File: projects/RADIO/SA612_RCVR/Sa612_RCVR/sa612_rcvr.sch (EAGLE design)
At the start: 33 parts, among them IC1 SA612AN, Q1 BC238

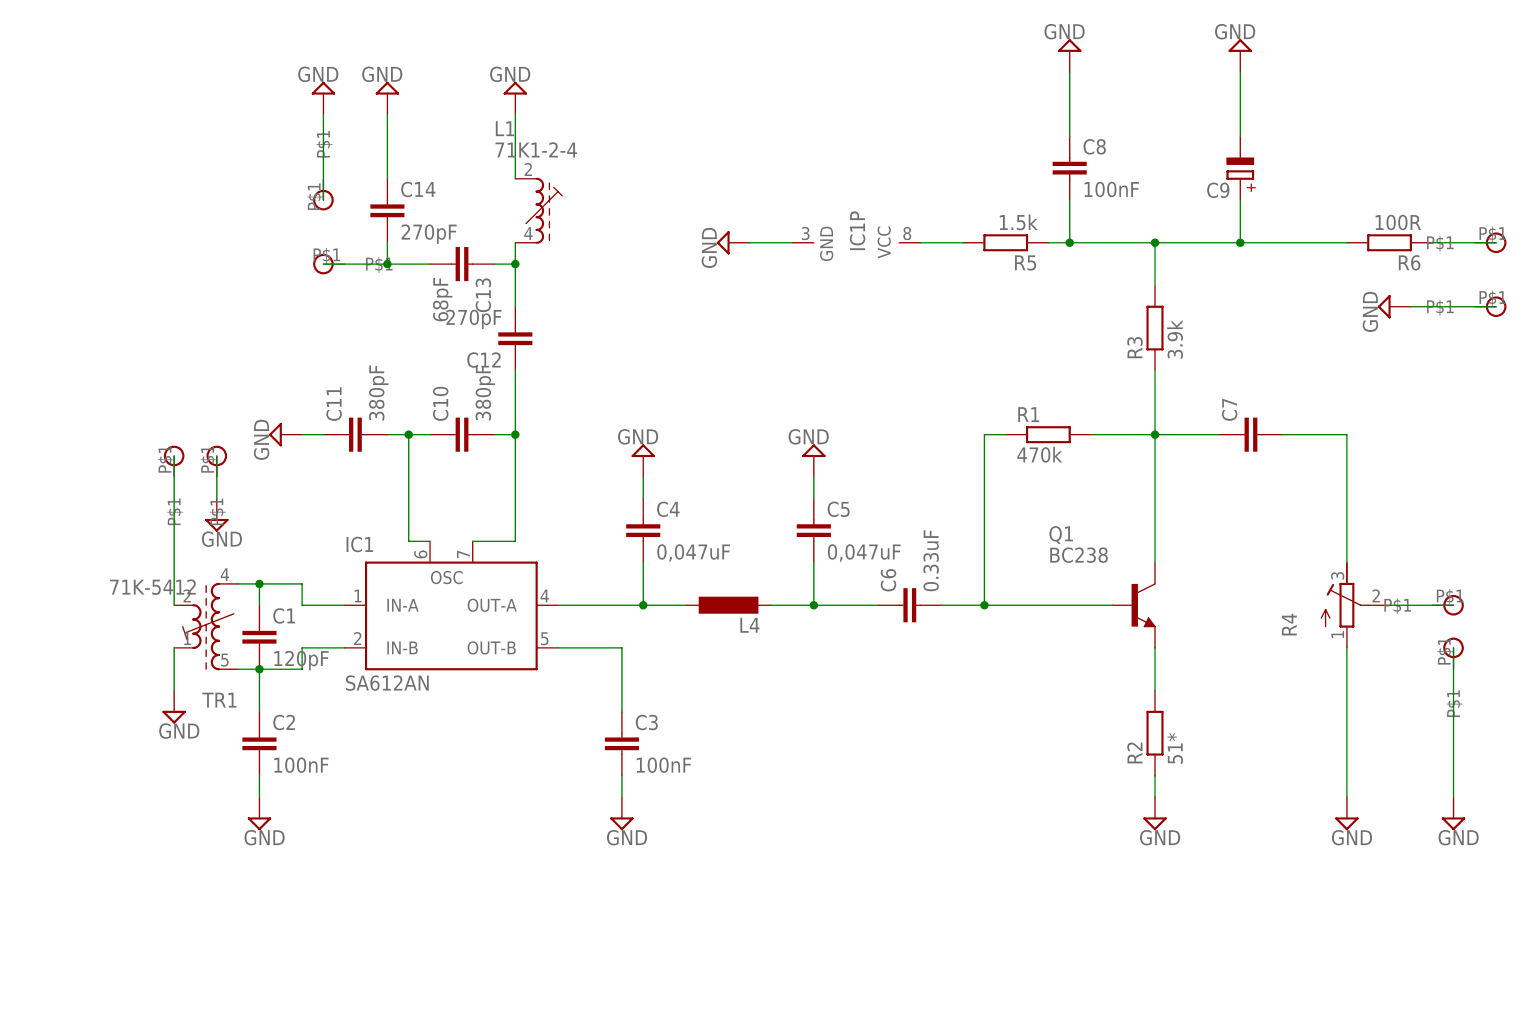
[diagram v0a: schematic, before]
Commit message: add sa612_SW_receiver
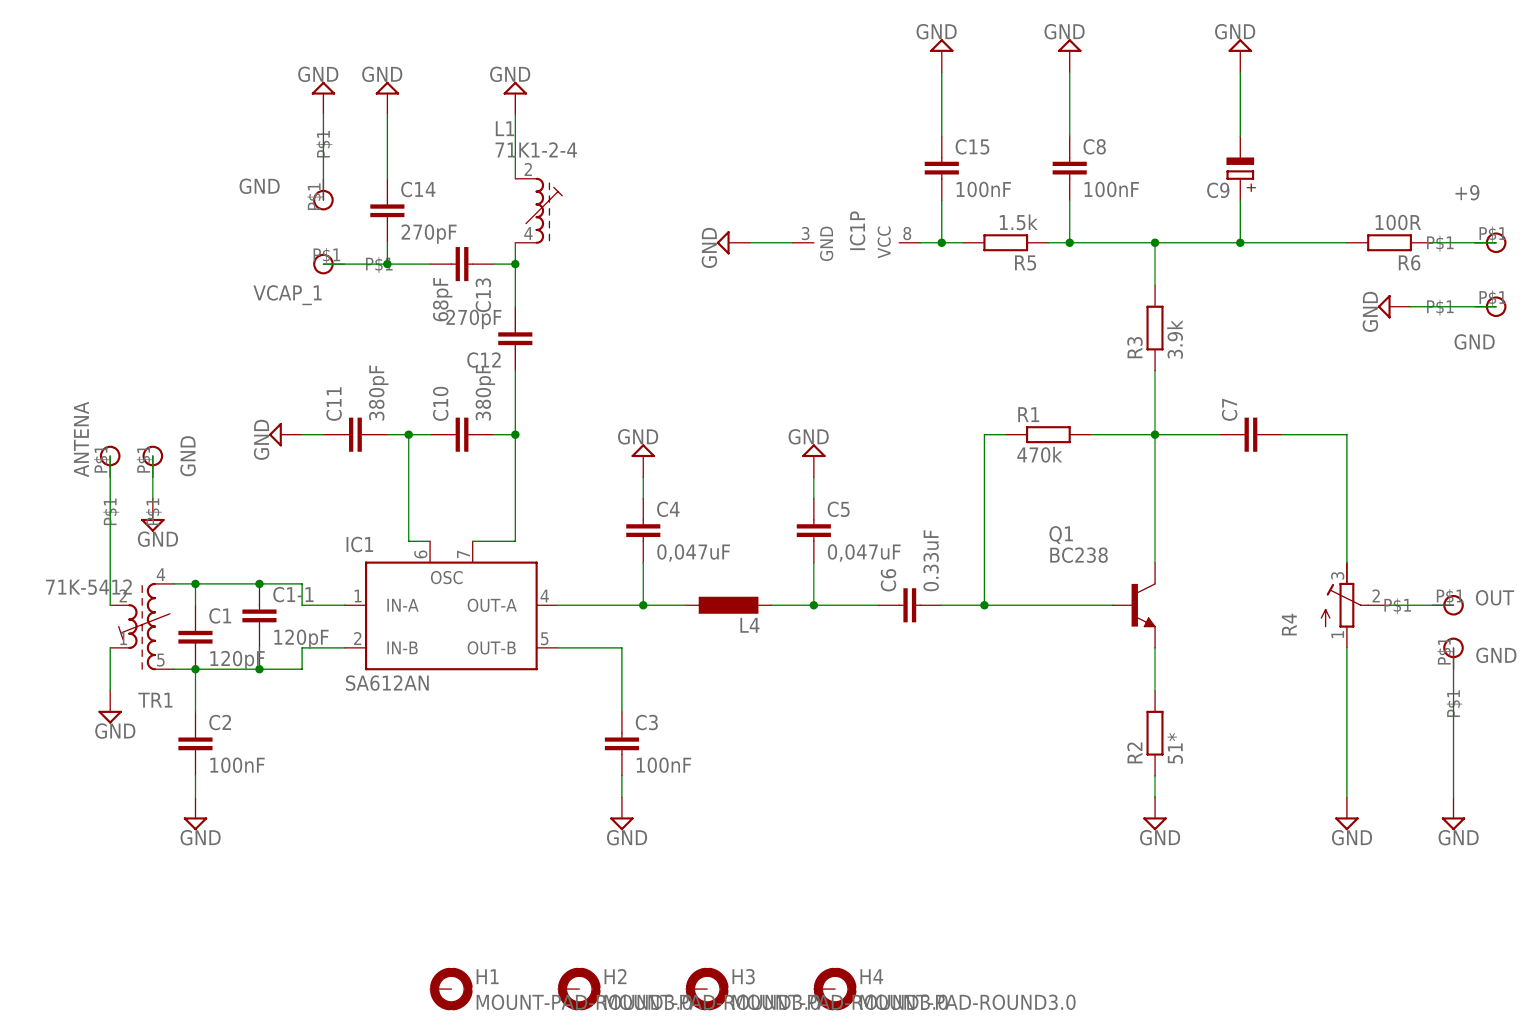
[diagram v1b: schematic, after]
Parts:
- added C1-1: 120pF, rcl:C-EU050-025X075
- added C15: 100nF, rcl:C-EUC0805K
- added H1, H2, H3, H4: MOUNT-PAD-ROUND3.0, holes:MOUNT-PAD-ROUND3.0
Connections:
- net N$11 renamed OUT
- net N$14 renamed +9
- net N$18 renamed VCAP_1
- net N$3 renamed ANTENA
- net GND: now also C15.1
- net N$1: now also C1-1.1
- net N$12: now also C15.2
- net N$2: now also C1-1.2
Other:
- moved on the sheet: C1, C2, TR1

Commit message: update
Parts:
- C7: device rcl:C-EU050-050X075 -> rcl:C-EU050-025X075
- TR1: value 71K-5412 -> 71K-1524; device inductor-neosid:71K-5412 -> inductor-neosid:71K-1524
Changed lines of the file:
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@@
 <parts>
 <part name="IC1" library="linear" library_urn="urn:adsk.eagle:library:262" deviceset="SA612A" device="N" package3d_urn="urn:adsk.eagle:package:16409/2"/>
-<part name="TR1" library="inductor-neosid" library_urn="urn:adsk.eagle:library:241" deviceset="71K-" device="5412" package3d_urn="urn:adsk.eagle:package:14718/1"/>
+<part name="TR1" library="inductor-neosid" deviceset="71K-" device="1524" package3d_urn="urn:adsk.eagle:package:14718/1"/>
 <part name="SUPPLY1" library="supply2" library_urn="urn:adsk.eagle:library:372" deviceset="GND" device=""/>
 <part name="SUPPLY2" library="supply2" library_urn="urn:adsk.eagle:library:372" deviceset="GND" device=""/>
@@
 <part name="R2" library="rcl" library_urn="urn:adsk.eagle:library:334" deviceset="R-EU_" device="R0805" package3d_urn="urn:adsk.eagle:package:23553/2" value="51*"/>
 <part name="R3" library="rcl" library_urn="urn:adsk.eagle:library:334" deviceset="R-EU_" device="R0805" package3d_urn="urn:adsk.eagle:package:23553/2" value="3.9k"/>
-<part name="C7" library="rcl" library_urn="urn:adsk.eagle:library:334" deviceset="C-EU" device="050-050X075" package3d_urn="urn:adsk.eagle:package:23665/1"/>
+<part name="C7" library="rcl" deviceset="C-EU" device="050-025X075" package3d_urn="urn:adsk.eagle:package:23637/1"/>
 <part name="R4" library="rcl" library_urn="urn:adsk.eagle:library:334" deviceset="R-TRIMM" device="64X" package3d_urn="urn:adsk.eagle:package:23749/1"/>
 <part name="SUPPLY7" library="supply2" library_urn="urn:adsk.eagle:library:372" deviceset="GND" device=""/>
@@
 <part name="U$8" library="mylib" deviceset="SMD_PIN" device=""/>
 <part name="SUPPLY17" library="supply2" library_urn="urn:adsk.eagle:library:372" deviceset="GND" device=""/>
-<part name="C1-1" library="rcl" library_urn="urn:adsk.eagle:library:334" deviceset="C-EU" device="050-025X075" package3d_urn="urn:adsk.eagle:package:23637/1" value="120pF"/>
+<part name="C1-1" library="rcl" deviceset="C-EU" device="050-025X075" package3d_urn="urn:adsk.eagle:package:23637/1" value="120pF"/>
 <part name="H1" library="holes" library_urn="urn:adsk.eagle:library:237" deviceset="MOUNT-PAD-ROUND" device="3.0" package3d_urn="urn:adsk.eagle:package:14280/1"/>
 <part name="H2" library="holes" library_urn="urn:adsk.eagle:library:237" deviceset="MOUNT-PAD-ROUND" device="3.0" package3d_urn="urn:adsk.eagle:package:14280/1"/>
